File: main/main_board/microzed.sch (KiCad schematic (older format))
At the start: 6 parts, among them U13 DS90LV048

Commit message: Mostly work on hooking in the Microzed using kipart symbols and a footprint. Also added 2.5V VCCIO regulator.
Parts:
- removed C47: 100nF, Capacitor_SMD:C_0603_1608Metric, symbol Device:C_Small
- removed R37, R38, R39: 100, Resistor_SMD:R_0603_1608Metric, symbol Device:R_US
- removed RN3: 33, Resistor_SMD:R_Array_Convex_4x0603, symbol Device:R_Pack04
- removed U13: DS90LV048, Package_SO:TSSOP-16_4.4x5mm_P0.65mm, symbol ilemt_input:FIN1048
- added C55, C56: 10uF, Capacitor_SMD:C_0603_1608Metric, symbol Device:C_Small
- added U6: AP3761C-25SP, Package_SO:SOIC-8-1EP_3.9x4.9mm_P1.27mm_EP2.41x3.3mm_ThermalVias, symbol AP3761C-xxSP:AP3761C-xxSP
- added X1: MicroZed, main_board:Microzed, symbol microzed:MicroZed
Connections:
- net labels added: +5_Zedboard, GNDD, PROBE_CONFIG, SCL, SDA
- net labels removed: FPGA_MCLK_ENA+, FPGA_MCLK_ENA-, FPGA_SCKA+, FPGA_SCKA-, FPGA_SCKB+, FPGA_SCKB-, GND, MCLK_ENA, OVDD, SCKA, SCKB
- wire segments 45 -> 31
- no-connect marks 0 -> 1

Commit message: Updated for new microzed pin mapping scheme.
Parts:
- X1: value MicroZed -> microzed; symbol microzed:MicroZed -> microzed:microzed
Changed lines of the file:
@@
 Comment4 ""
 $EndDescr
-$Comp
-L microzed:MicroZed X1
-U 9 1 5F30DCC7
-P 5350 1750
-AR Path="/5F30DCC7" Ref="X1"  Part="9"
-AR Path="/5E525F87/5F30DCC7" Ref="X1"  Part="9"
-F 0 "X1" H 5550 2000 60  0000 L CNN
-F 1 "MicroZed" H 5550 1900 60  0000 L CNN
-F 2 "main_board:Microzed" H 5550 1800 60  0001 L CNN
-F 3 "" H 5550 1600 60  0001 L CNN
-	9    5350 1750
-	1    0    0    -1
-$EndComp
-NoConn ~ 5350 1750
+NoConn ~ 5350 2050
 $Comp
 L power:GNDD #PWR044
@@
 	5300 2250 5300 2350
 $Comp
-L microzed:MicroZed X1
-U 10 1 5EDF12A5
+L microzed:microzed X1
+U 12 1 5EDF12A5
 P 7950 1750
-F 0 "X1" H 8150 2000 60  0000 L CNN
-F 1 "MicroZed" H 8150 1900 60  0000 L CNN
+AR Path="/5EDF12A5" Ref="X1"  Part="10"
+AR Path="/5E525F87/5EDF12A5" Ref="M1"  Part="12"
+F 0 "M1" H 8150 2000 60  0000 L CNN
+F 1 "microzed" H 8150 1900 60  0000 L CNN
 F 2 "main_board:Microzed" H 8150 1800 60  0001 L CNN
 F 3 "" H 8150 1600 60  0001 L CNN
-	10   7950 1750
+	12   7950 1750
 	1    0    0    -1
 $EndComp
@@
 	2200 3100 3000 3100
 Wire Wire Line
-	5250 1850 5250 2050
-Wire Wire Line
-	5250 2050 5350 2050
-Wire Wire Line
 	3950 3200 3950 3100
 Connection ~ 3950 3100
@@
 	2200 2250 2200 2700
 Wire Wire Line
-	6850 2050 7050 2050
+	6850 2150 7050 2150
 Wire Wire Line
 	1800 2350 2400 2350
@@
 Connection ~ 5300 2350
 Wire Wire Line
-	5250 1850 2200 1850
+	4850 1850 2200 1850
 Connection ~ 2200 1850
 Wire Wire Line
 	1800 3550 7050 3550
 Wire Wire Line
-	7050 2050 7050 3550
+	1800 3550 1800 2350
+$Comp
+L microzed:microzed X1
+U 11 1 5F30DCC7
+P 5350 1850
+AR Path="/5F30DCC7" Ref="X1"  Part="9"
+AR Path="/5E525F87/5F30DCC7" Ref="M1"  Part="11"
+F 0 "M1" H 5550 2100 60  0000 L CNN
+F 1 "microzed" H 5550 2000 60  0000 L CNN
+F 2 "main_board:Microzed" H 5550 1900 60  0001 L CNN
+F 3 "" H 5550 1700 60  0001 L CNN
+	11   5350 1850
+	1    0    0    -1
+$EndComp
 Wire Wire Line
-	1800 3550 1800 2350
+	4850 1850 4850 2450
+Wire Wire Line
+	4850 2450 5350 2450
+Wire Wire Line
+	7050 2150 7050 3550
 $EndSCHEMATC

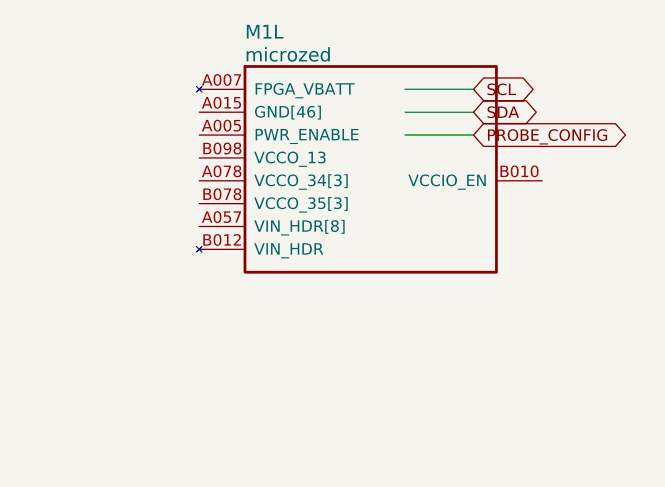
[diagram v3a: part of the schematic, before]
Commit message: Schematic is mostly complete (except for BIST DACs), and passes ERC.  Rough placement of components on PCB.
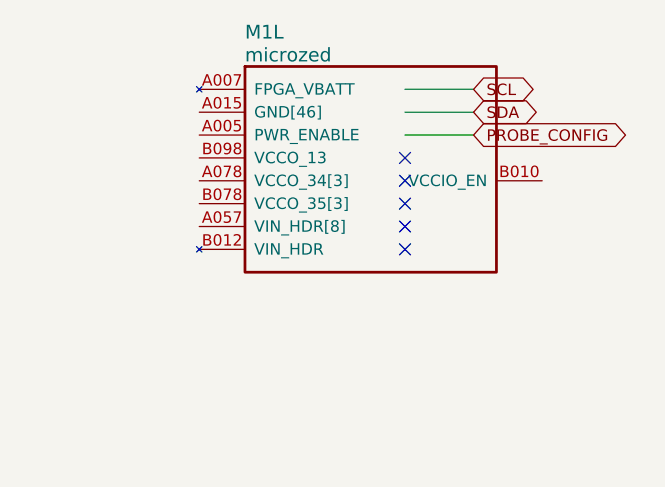
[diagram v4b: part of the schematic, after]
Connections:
- no-connect marks 1 -> 6
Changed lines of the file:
@@
 Wire Wire Line
 	7050 2150 7050 3550
+NoConn ~ 8850 2050
+NoConn ~ 8850 2150
+NoConn ~ 8850 2250
+NoConn ~ 8850 2350
+NoConn ~ 8850 2450
 $EndSCHEMATC

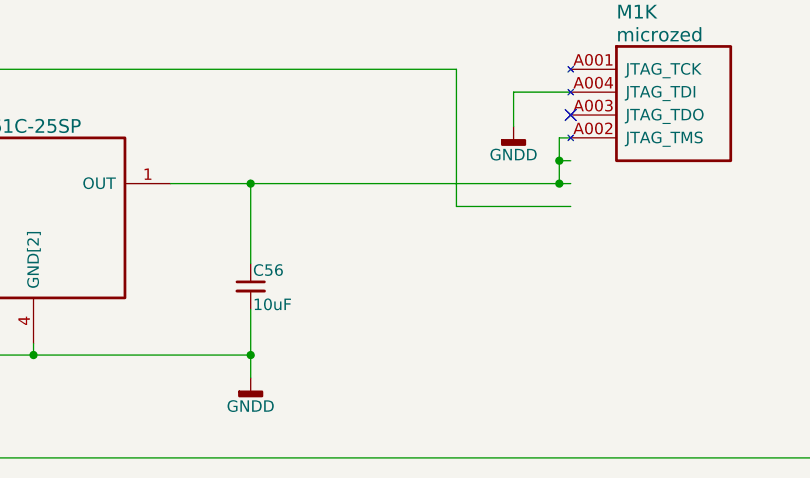
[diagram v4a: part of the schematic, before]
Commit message: Mostly work on main board layout. Aligned things on mm grid for easier routing, moved things around to create routing area. Neatened up component groups onto the grid. Parts of the routing plan are now drawn on the PCB.  See also notebook.txt. Reduced pad size of the PCIE connector, tweaked design rule clearances. Minor schematic tweaks.
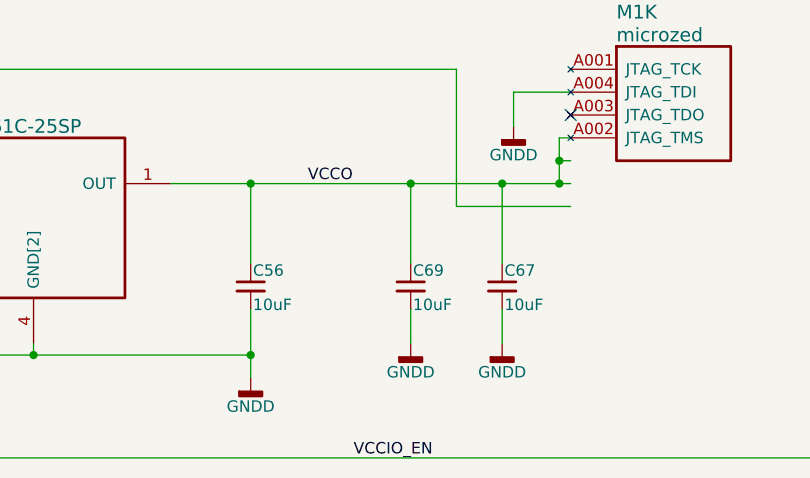
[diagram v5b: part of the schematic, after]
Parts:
- added C67, C69: 10uF, Capacitor_SMD:C_0603_1608Metric, symbol Device:C_Small
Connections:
- net labels added: VCCIO_EN, VCCO
- wire segments 31 -> 37
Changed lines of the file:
@@
 	1    0    0    -1
 $EndComp
+Wire Wire Line
+	3950 2900 3950 3100
+Connection ~ 3000 3100
+Wire Wire Line
+	3000 3100 3000 3050
+Wire Wire Line
+	3950 2700 3950 2350
+$Comp
+L Device:C_Small C?
+U 1 1 5EE25BE6
+P 2200 2800
+AR Path="/5DFCF14D/5DA78AA2/5EE25BE6" Ref="C?"  Part="1"
+AR Path="/5DFCF14D/5E295469/5EE25BE6" Ref="C?"  Part="1"
+AR Path="/5E448095/5DA78AA2/5EE25BE6" Ref="C?"  Part="1"
+AR Path="/5E45936E/5DA78AA2/5EE25BE6" Ref="C?"  Part="1"
+AR Path="/5E525F2C/5E6427A0/5DA78AA2/5EE25BE6" Ref="C?"  Part="1"
+AR Path="/5E624B3C/5DFCF14D/5DA78AA2/5EE25BE6" Ref="C?"  Part="1"
+AR Path="/5E624B3C/5E448095/5DA78AA2/5EE25BE6" Ref="C?"  Part="1"
+AR Path="/5E624B3C/5E45936E/5DA78AA2/5EE25BE6" Ref="C?"  Part="1"
+AR Path="/5E525F2C/5EE25BE6" Ref="C?"  Part="1"
+AR Path="/5E525FC9/5EE25BE6" Ref="C?"  Part="1"
+AR Path="/5E525F87/5EE25BE6" Ref="C55"  Part="1"
+F 0 "C55" H 2210 2870 50  0000 L CNN
+F 1 "10uF" H 2210 2720 50  0000 L CNN
+F 2 "Capacitor_SMD:C_0603_1608Metric" H 2200 2800 50  0001 C CNN
+F 3 "http://datasheets.avx.com/cx5r.pdf" H 2200 2800 50  0001 C CNN
+F 4 "CAP CER 10UF 6.3V X5R 0603" H 2200 2800 50  0001 C CNN "Description"
+F 5 "478-5318-1-ND" H 2200 2800 50  0001 C CNN "Digikey"
+F 6 "06036D106MAT2A" H 2200 2800 50  0001 C CNN "MPN"
+F 7 "29" H 2200 2800 50  0001 C CNN "DK line"
+	1    2200 2800
+	1    0    0    -1
+$EndComp
+Wire Wire Line
+	2200 2900 2200 3100
+Wire Wire Line
+	2200 3100 3000 3100
+Wire Wire Line
+	3950 3200 3950 3100
+Connection ~ 3950 3100
+Wire Wire Line
+	2200 1850 2200 2250
+Wire Wire Line
+	3000 3100 3950 3100
+Wire Wire Line
+	2400 2250 2200 2250
+Connection ~ 2200 2250
+Wire Wire Line
+	2200 2250 2200 2700
+Wire Wire Line
+	6850 2150 7050 2150
+Wire Wire Line
+	1800 2350 2400 2350
+Wire Wire Line
+	3950 2350 4650 2350
+Connection ~ 3950 2350
+Connection ~ 5300 2350
+Wire Wire Line
+	4850 1850 2200 1850
+Connection ~ 2200 1850
+Wire Wire Line
+	1800 3550 7050 3550
+Wire Wire Line
+	1800 3550 1800 2350
+$Comp
+L microzed:microzed X1
+U 11 1 5F30DCC7
+P 5350 1850
+AR Path="/5F30DCC7" Ref="X1"  Part="9"
+AR Path="/5E525F87/5F30DCC7" Ref="M1"  Part="11"
+F 0 "M1" H 5550 2100 60  0000 L CNN
+F 1 "microzed" H 5550 2000 60  0000 L CNN
+F 2 "main_board:Microzed" H 5550 1900 60  0001 L CNN
+F 3 "" H 5550 1700 60  0001 L CNN
+	11   5350 1850
+	1    0    0    -1
+$EndComp
+Wire Wire Line
+	4850 1850 4850 2450
+Wire Wire Line
+	4850 2450 5350 2450
+Wire Wire Line
+	7050 2150 7050 3550
+NoConn ~ 8850 2050
+NoConn ~ 8850 2150
+NoConn ~ 8850 2250
+NoConn ~ 8850 2350
+NoConn ~ 8850 2450
+Text Label 4200 2350 0    50   ~ 0
+VCCO
+Text Label 4400 3550 0    50   ~ 0
+VCCIO_EN
 $Comp
 L Device:C_Small C?
@@
 	1    0    0    -1
 $EndComp
-Wire Wire Line
-	3950 2900 3950 3100
-Connection ~ 3000 3100
-Wire Wire Line
-	3000 3100 3000 3050
-Wire Wire Line
-	3950 2700 3950 2350
-$Comp
-L Device:C_Small C?
-U 1 1 5EE25BE6
-P 2200 2800
-AR Path="/5DFCF14D/5DA78AA2/5EE25BE6" Ref="C?"  Part="1"
-AR Path="/5DFCF14D/5E295469/5EE25BE6" Ref="C?"  Part="1"
-AR Path="/5E448095/5DA78AA2/5EE25BE6" Ref="C?"  Part="1"
-AR Path="/5E45936E/5DA78AA2/5EE25BE6" Ref="C?"  Part="1"
-AR Path="/5E525F2C/5E6427A0/5DA78AA2/5EE25BE6" Ref="C?"  Part="1"
-AR Path="/5E624B3C/5DFCF14D/5DA78AA2/5EE25BE6" Ref="C?"  Part="1"
-AR Path="/5E624B3C/5E448095/5DA78AA2/5EE25BE6" Ref="C?"  Part="1"
-AR Path="/5E624B3C/5E45936E/5DA78AA2/5EE25BE6" Ref="C?"  Part="1"
-AR Path="/5E525F2C/5EE25BE6" Ref="C?"  Part="1"
-AR Path="/5E525FC9/5EE25BE6" Ref="C?"  Part="1"
-AR Path="/5E525F87/5EE25BE6" Ref="C55"  Part="1"
-F 0 "C55" H 2210 2870 50  0000 L CNN
-F 1 "10uF" H 2210 2720 50  0000 L CNN
-F 2 "Capacitor_SMD:C_0603_1608Metric" H 2200 2800 50  0001 C CNN
-F 3 "http://datasheets.avx.com/cx5r.pdf" H 2200 2800 50  0001 C CNN
-F 4 "CAP CER 10UF 6.3V X5R 0603" H 2200 2800 50  0001 C CNN "Description"
-F 5 "478-5318-1-ND" H 2200 2800 50  0001 C CNN "Digikey"
-F 6 "06036D106MAT2A" H 2200 2800 50  0001 C CNN "MPN"
-F 7 "29" H 2200 2800 50  0001 C CNN "DK line"
-	1    2200 2800
-	1    0    0    -1
-$EndComp
-Wire Wire Line
-	2200 2900 2200 3100
-Wire Wire Line
-	2200 3100 3000 3100
-Wire Wire Line
-	3950 3200 3950 3100
-Connection ~ 3950 3100
-Wire Wire Line
-	2200 1850 2200 2250
-Wire Wire Line
-	3000 3100 3950 3100
-Wire Wire Line
-	2400 2250 2200 2250
-Connection ~ 2200 2250
-Wire Wire Line
-	2200 2250 2200 2700
-Wire Wire Line
-	6850 2150 7050 2150
-Wire Wire Line
-	1800 2350 2400 2350
-Wire Wire Line
-	3950 2350 5300 2350
-Connection ~ 3950 2350
-Connection ~ 5300 2350
-Wire Wire Line
-	4850 1850 2200 1850
-Connection ~ 2200 1850
-Wire Wire Line
-	1800 3550 7050 3550
-Wire Wire Line
-	1800 3550 1800 2350
-$Comp
-L microzed:microzed X1
-U 11 1 5F30DCC7
-P 5350 1850
-AR Path="/5F30DCC7" Ref="X1"  Part="9"
-AR Path="/5E525F87/5F30DCC7" Ref="M1"  Part="11"
-F 0 "M1" H 5550 2100 60  0000 L CNN
-F 1 "microzed" H 5550 2000 60  0000 L CNN
-F 2 "main_board:Microzed" H 5550 1900 60  0001 L CNN
-F 3 "" H 5550 1700 60  0001 L CNN
-	11   5350 1850
-	1    0    0    -1
-$EndComp
-Wire Wire Line
-	4850 1850 4850 2450
-Wire Wire Line
-	4850 2450 5350 2450
-Wire Wire Line
-	7050 2150 7050 3550
-NoConn ~ 8850 2050
-NoConn ~ 8850 2150
-NoConn ~ 8850 2250
-NoConn ~ 8850 2350
-NoConn ~ 8850 2450
+$Comp
+L Device:C_Small C?
+U 1 1 5F0CDEE8
+P 5050 2800
+AR Path="/5DFCF14D/5DA78AA2/5F0CDEE8" Ref="C?"  Part="1"
+AR Path="/5DFCF14D/5E295469/5F0CDEE8" Ref="C?"  Part="1"
+AR Path="/5E448095/5DA78AA2/5F0CDEE8" Ref="C?"  Part="1"
+AR Path="/5E45936E/5DA78AA2/5F0CDEE8" Ref="C?"  Part="1"
+AR Path="/5E525F2C/5E6427A0/5DA78AA2/5F0CDEE8" Ref="C?"  Part="1"
+AR Path="/5E624B3C/5DFCF14D/5DA78AA2/5F0CDEE8" Ref="C?"  Part="1"
+AR Path="/5E624B3C/5E448095/5DA78AA2/5F0CDEE8" Ref="C?"  Part="1"
+AR Path="/5E624B3C/5E45936E/5DA78AA2/5F0CDEE8" Ref="C?"  Part="1"
+AR Path="/5E525F2C/5F0CDEE8" Ref="C?"  Part="1"
+AR Path="/5E525FC9/5F0CDEE8" Ref="C?"  Part="1"
+AR Path="/5E525F87/5F0CDEE8" Ref="C67"  Part="1"
+F 0 "C67" H 5060 2870 50  0000 L CNN
+F 1 "10uF" H 5060 2720 50  0000 L CNN
+F 2 "Capacitor_SMD:C_0603_1608Metric" H 5050 2800 50  0001 C CNN
+F 3 "http://datasheets.avx.com/cx5r.pdf" H 5050 2800 50  0001 C CNN
+F 4 "CAP CER 10UF 6.3V X5R 0603" H 5050 2800 50  0001 C CNN "Description"
+F 5 "478-5318-1-ND" H 5050 2800 50  0001 C CNN "Digikey"
+F 6 "06036D106MAT2A" H 5050 2800 50  0001 C CNN "MPN"
+F 7 "29" H 5050 2800 50  0001 C CNN "DK line"
+	1    5050 2800
+	1    0    0    -1
+$EndComp
+Wire Wire Line
+	5050 2700 5050 2350
+Connection ~ 5050 2350
+Wire Wire Line
+	5050 2350 5300 2350
+$Comp
+L power:GNDD #PWR0124
+U 1 1 5F0CEF6D
+P 5050 3050
+F 0 "#PWR0124" H 5050 2800 50  0001 C CNN
+F 1 "GNDD" H 5050 2925 50  0000 C CNN
+F 2 "" H 5050 3050 50  0001 C CNN
+F 3 "" H 5050 3050 50  0001 C CNN
+	1    5050 3050
+	1    0    0    -1
+$EndComp
+Wire Wire Line
+	5050 2900 5050 3050
+$Comp
+L Device:C_Small C?
+U 1 1 5F0F5DEB
+P 4650 2800
+AR Path="/5DFCF14D/5DA78AA2/5F0F5DEB" Ref="C?"  Part="1"
+AR Path="/5DFCF14D/5E295469/5F0F5DEB" Ref="C?"  Part="1"
+AR Path="/5E448095/5DA78AA2/5F0F5DEB" Ref="C?"  Part="1"
+AR Path="/5E45936E/5DA78AA2/5F0F5DEB" Ref="C?"  Part="1"
+AR Path="/5E525F2C/5E6427A0/5DA78AA2/5F0F5DEB" Ref="C?"  Part="1"
+AR Path="/5E624B3C/5DFCF14D/5DA78AA2/5F0F5DEB" Ref="C?"  Part="1"
+AR Path="/5E624B3C/5E448095/5DA78AA2/5F0F5DEB" Ref="C?"  Part="1"
+AR Path="/5E624B3C/5E45936E/5DA78AA2/5F0F5DEB" Ref="C?"  Part="1"
+AR Path="/5E525F2C/5F0F5DEB" Ref="C?"  Part="1"
+AR Path="/5E525FC9/5F0F5DEB" Ref="C?"  Part="1"
+AR Path="/5E525F87/5F0F5DEB" Ref="C69"  Part="1"
+F 0 "C69" H 4660 2870 50  0000 L CNN
+F 1 "10uF" H 4660 2720 50  0000 L CNN
+F 2 "Capacitor_SMD:C_0603_1608Metric" H 4650 2800 50  0001 C CNN
+F 3 "http://datasheets.avx.com/cx5r.pdf" H 4650 2800 50  0001 C CNN
+F 4 "CAP CER 10UF 6.3V X5R 0603" H 4650 2800 50  0001 C CNN "Description"
+F 5 "478-5318-1-ND" H 4650 2800 50  0001 C CNN "Digikey"
+F 6 "06036D106MAT2A" H 4650 2800 50  0001 C CNN "MPN"
+F 7 "29" H 4650 2800 50  0001 C CNN "DK line"
+	1    4650 2800
+	1    0    0    -1
+$EndComp
+$Comp
+L power:GNDD #PWR0126
+U 1 1 5F0F5DF2
+P 4650 3050
+F 0 "#PWR0126" H 4650 2800 50  0001 C CNN
+F 1 "GNDD" H 4650 2925 50  0000 C CNN
+F 2 "" H 4650 3050 50  0001 C CNN
+F 3 "" H 4650 3050 50  0001 C CNN
+	1    4650 3050
+	1    0    0    -1
+$EndComp
+Wire Wire Line
+	4650 2900 4650 3050
+Wire Wire Line
+	4650 2700 4650 2350
+Connection ~ 4650 2350
+Wire Wire Line
+	4650 2350 5050 2350
 $EndSCHEMATC

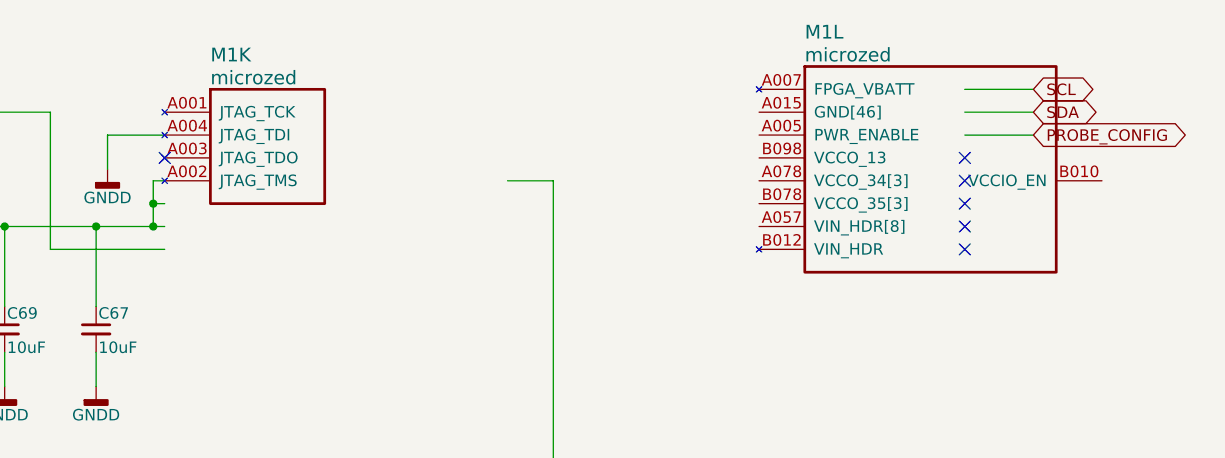
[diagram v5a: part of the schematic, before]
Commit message: Changes related to pin mapping. There's a new BIST unit in the Microzed symbol, and the unit ordering has changed. I also added SDI lines to the input slots which could be used to configure the ADC in a future version of the input board. Added some wire labels for easier routing.
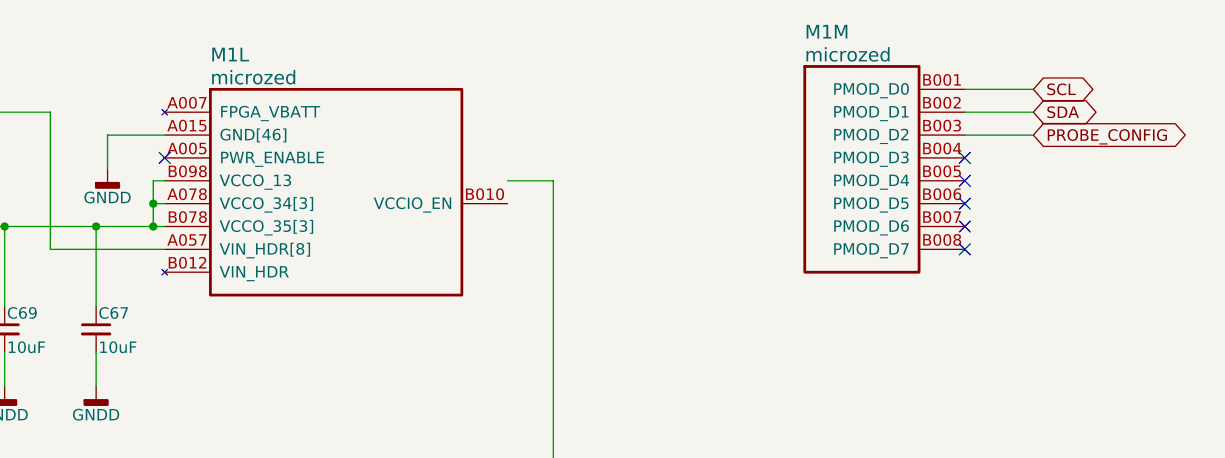
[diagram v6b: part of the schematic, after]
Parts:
- removed unit 11 of X1
- added M1: microzed, main_board:Microzed, symbol microzed:microzed
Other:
- moved on the sheet: M1L
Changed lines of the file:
@@
 L microzed:microzed X1
 U 12 1 5EDF12A5
-P 7950 1750
+P 5350 1850
 AR Path="/5EDF12A5" Ref="X1"  Part="10"
 AR Path="/5E525F87/5EDF12A5" Ref="M1"  Part="12"
-F 0 "M1" H 8150 2000 60  0000 L CNN
-F 1 "microzed" H 8150 1900 60  0000 L CNN
-F 2 "main_board:Microzed" H 8150 1800 60  0001 L CNN
-F 3 "" H 8150 1600 60  0001 L CNN
-	12   7950 1750
+F 0 "M1" H 5550 2100 60  0000 L CNN
+F 1 "microzed" H 5550 2000 60  0000 L CNN
+F 2 "main_board:Microzed" H 5550 1900 60  0001 L CNN
+F 3 "" H 5550 1700 60  0001 L CNN
+	12   5350 1850
 	1    0    0    -1
 $EndComp
@@
 Wire Wire Line
 	1800 3550 1800 2350
-$Comp
-L microzed:microzed X1
-U 11 1 5F30DCC7
-P 5350 1850
-AR Path="/5F30DCC7" Ref="X1"  Part="9"
-AR Path="/5E525F87/5F30DCC7" Ref="M1"  Part="11"
-F 0 "M1" H 5550 2100 60  0000 L CNN
-F 1 "microzed" H 5550 2000 60  0000 L CNN
-F 2 "main_board:Microzed" H 5550 1900 60  0001 L CNN
-F 3 "" H 5550 1700 60  0001 L CNN
-	11   5350 1850
-	1    0    0    -1
-$EndComp
 Wire Wire Line
 	4850 1850 4850 2450
@@
 Wire Wire Line
 	4650 2350 5050 2350
+$Comp
+L microzed:microzed M1
+U 13 1 5F181B21
+P 7950 1750
+F 0 "M1" H 8150 2000 60  0000 L CNN
+F 1 "microzed" H 8150 1900 60  0000 L CNN
+F 2 "main_board:Microzed" H 8150 1800 60  0001 L CNN
+F 3 "" H 8150 1600 60  0001 L CNN
+	13   7950 1750
+	1    0    0    -1
+$EndComp
 $EndSCHEMATC
